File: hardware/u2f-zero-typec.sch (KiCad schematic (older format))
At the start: 18 parts, among them J1 USBTypeC, SW1 SW_PUSH

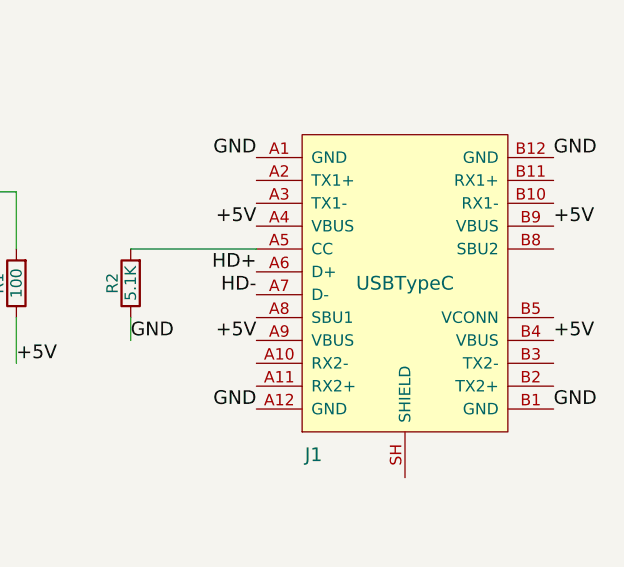
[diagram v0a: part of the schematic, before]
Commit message: add connector models
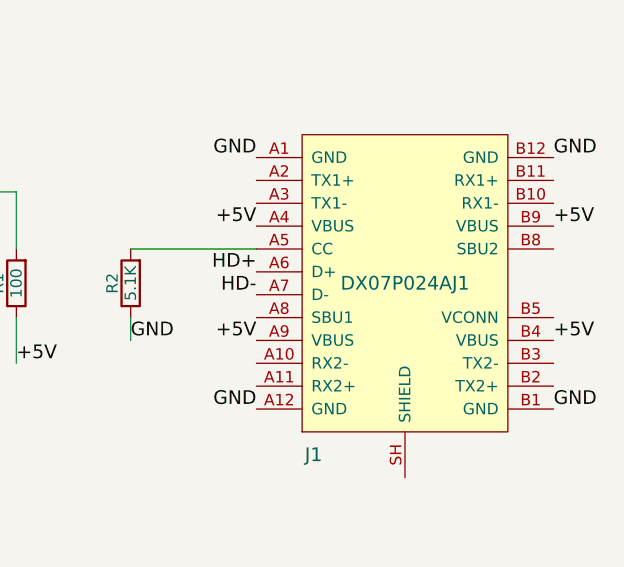
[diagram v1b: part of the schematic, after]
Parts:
- J1: value USBTypeC -> DX07P024AJ1
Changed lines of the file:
@@
 LIBS:siliconlabs
 LIBS:u2f-zero-rescue
-LIBS:u2f-zero-typec-cache
+LIBS:u2f-zero-cache
 EELAYER 25 0
 EELAYER END
@@
 P 9350 5550
 F 0 "J1" H 9400 5450 60  0000 C CNN
-F 1 "USBTypeC" H 9800 6200 60  0000 C CNN
+F 1 "DX07P024AJ1" H 9800 6200 60  0000 C CNN
 F 2 "footprints:USB-TypeC-Male" H 9350 5550 60  0001 C CNN
 F 3 "http://www.jae.com/z-en/pdf_download_exec.cfm?param=SJ116680.pdf" H 9350 5550 60  0001 C CNN
